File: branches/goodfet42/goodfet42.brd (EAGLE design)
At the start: 47.9 x 19.7 mm, 11 parts, among them U1 F261X---PM64, U2 FT232RL-BASICSSOP

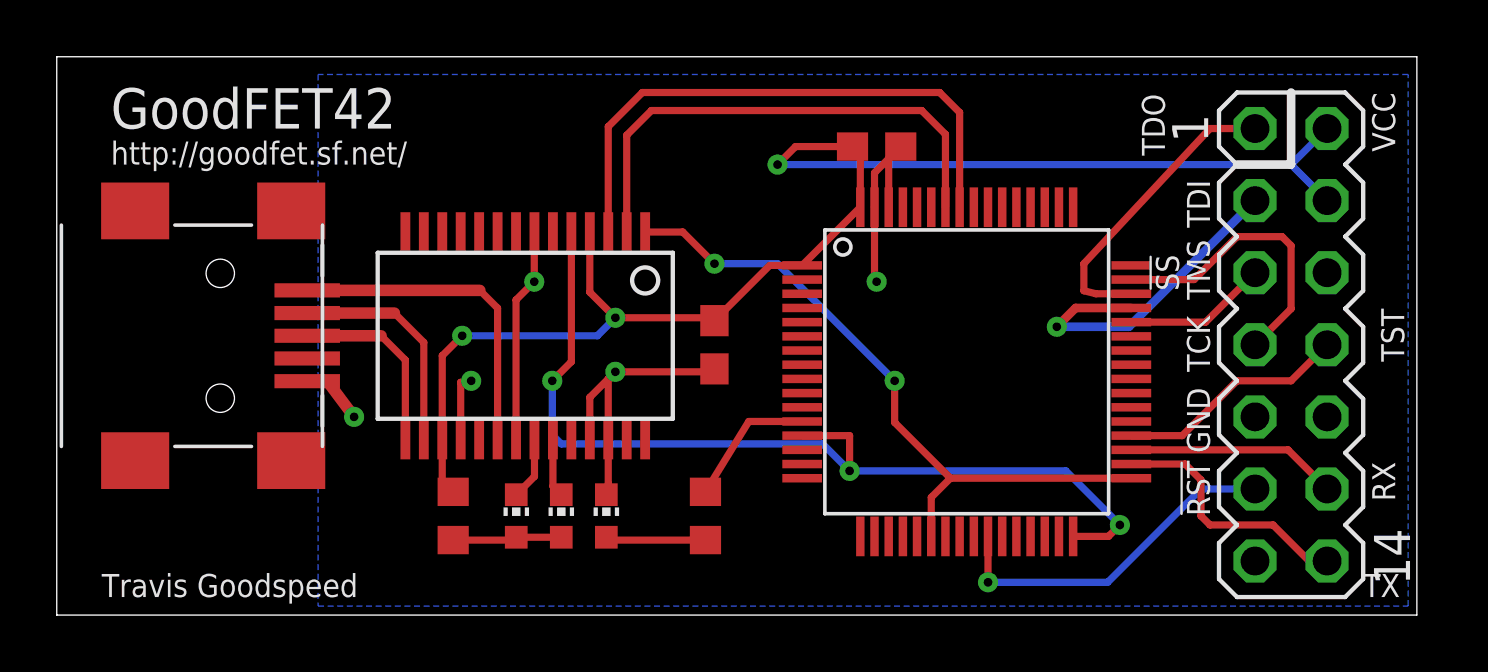
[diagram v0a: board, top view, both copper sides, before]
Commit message: Reinserted names, values in layout.
git-svn-id: https://svn.code.sf.net/p/goodfet/code@1316 12e2690d-a6be-4b82-a7b7-67c4a43b65c8
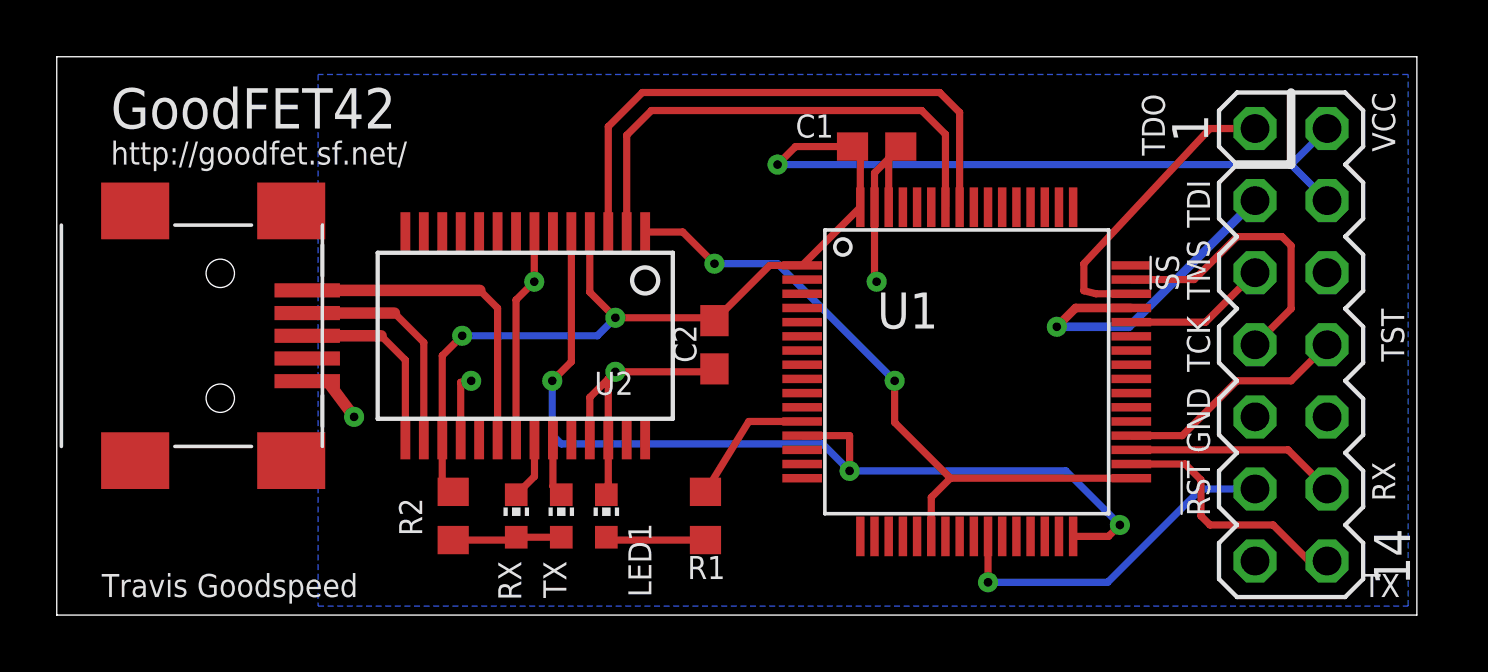
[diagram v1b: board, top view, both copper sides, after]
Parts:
- U1: value F261X---PM64 -> MSP430F2618TPM
- U2: value FT232RL-BASICSSOP -> FT232RL
- renumbered RXLED to RX, TXLED to TX
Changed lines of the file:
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@@
 <?xml version="1.0" encoding="utf-8"?>
 <!DOCTYPE eagle SYSTEM "eagle.dtd">
-<eagle version="6.2">
+<eagle version="6.3">
 <drawing>
 <settings>
@@
 </class>
 </classes>
-<designrules>
+<designrules name="default">
 <description language="de">&lt;b&gt;EAGLE Design Rules&lt;/b&gt;
 &lt;p&gt;
@@
 </autorouter>
 <elements>
-<element name="C1" library="rcl" package="C0603" value="0.1µF" x="28.8925" y="16.51" smashed="yes" rot="R180"/>
-<element name="R1" library="rcl" package="R0603" value="330" x="22.86" y="3.4925" smashed="yes" rot="R90"/>
+<element name="C1" library="rcl" package="C0603" value="0.1µF" x="28.8925" y="16.51" smashed="yes" rot="R180">
+<attribute name="NAME" x="26.035" y="16.8275" size="0.8128" layer="25" font="fixed"/>
+<attribute name="VALUE" x="30.7975" y="18.415" size="0.8128" layer="27" font="fixed" rot="R180"/>
+</element>
+<element name="R1" library="rcl" package="R0603" value="330" x="22.86" y="3.4925" smashed="yes" rot="R90">
+<attribute name="NAME" x="22.225" y="1.27" size="0.8128" layer="25" font="fixed"/>
+<attribute name="VALUE" x="24.13" y="1.27" size="0.8128" layer="27" font="fixed"/>
+</element>
 <element name="LED1" library="led" package="CHIP-LED0603" value="" x="19.3675" y="3.4925" smashed="yes">
+<attribute name="NAME" x="20.955" y="0.635" size="0.8128" layer="25" rot="R90"/>
 <attribute name="VALUE" x="21.2725" y="2.8575" size="1.27" layer="27" rot="R90"/>
 </element>
-<element name="U2" library="SparkFun" package="SSOP28DB" value="FT232RL-BASICSSOP" x="16.51" y="9.8425" smashed="yes" rot="R180"/>
-<element name="RXLED" library="led" package="CHIP-LED0603" value="" x="16.1925" y="3.4925" smashed="yes">
+<element name="U2" library="SparkFun" package="SSOP28DB" value="FT232RL" x="16.51" y="9.8425" smashed="yes" rot="R180">
+<attribute name="NAME" x="20.32" y="8.5725" size="0.8128" layer="25" font="fixed" rot="R180"/>
+<attribute name="VALUE" x="11.7475" y="11.43" size="0.8128" layer="27" font="fixed"/>
+</element>
+<element name="RX" library="led" package="CHIP-LED0603" value="" x="16.1925" y="3.4925" smashed="yes">
+<attribute name="NAME" x="15.5575" y="1.905" size="0.8128" layer="25" font="fixed" rot="R270"/>
 <attribute name="VALUE" x="18.0975" y="2.8575" size="1.27" layer="27" rot="R90"/>
 </element>
-<element name="TXLED" library="led" package="CHIP-LED0603" value="" x="17.78" y="3.4925" smashed="yes">
+<element name="TX" library="led" package="CHIP-LED0603" value="" x="17.78" y="3.4925" smashed="yes">
+<attribute name="NAME" x="17.145" y="1.905" size="0.8128" layer="25" font="fixed" rot="R270"/>
 <attribute name="VALUE" x="19.685" y="2.8575" size="1.27" layer="27" rot="R90"/>
 </element>
-<element name="R2" library="rcl" package="R0603" value="330" x="13.97" y="3.4925" smashed="yes" rot="R90"/>
-<element name="C2" library="rcl" package="C0603" value="0.1µF" x="23.1775" y="9.525" smashed="yes" rot="R90"/>
+<element name="R2" library="rcl" package="R0603" value="330" x="13.97" y="3.4925" smashed="yes" rot="R90">
+<attribute name="NAME" x="12.065" y="4.1275" size="0.8128" layer="25" font="fixed" rot="R270"/>
+<attribute name="VALUE" x="14.9225" y="1.905" size="0.8128" layer="27" rot="R180"/>
+</element>
+<element name="C2" library="rcl" package="C0603" value="0.1µF" x="23.1775" y="9.525" smashed="yes" rot="R90">
+<attribute name="NAME" x="22.5425" y="8.89" size="0.8128" layer="25" font="fixed" rot="R90"/>
+<attribute name="VALUE" x="25.0825" y="7.62" size="0.8128" layer="27" font="fixed" rot="R90"/>
+</element>
 <element name="JTAG" library="con-lstb" package="MA07-2" value="" x="43.4975" y="9.525" smashed="yes" rot="R270">
 <attribute name="VALUE" x="39.3065" y="12.065" size="1.27" layer="27" ratio="10" rot="R270"/>
 </element>
-<element name="U1" library="TI_MSP430_v13" package="PM/PAG64" value="F261X---PM64" x="32.0675" y="8.5725" smashed="yes"/>
+<element name="U1" library="TI_MSP430_v13" package="PM/PAG64" value="MSP430F2618TPM" x="32.0675" y="8.5725" smashed="yes">
+<attribute name="VALUE" x="27.2575" y="6.575" size="0.8128" layer="27" font="fixed" ratio="10"/>
+<attribute name="NAME" x="28.9125" y="10.0975" size="1.27" layer="25" font="fixed" ratio="10"/>
+</element>
 <element name="CN1" library="adafruit" package="USB-MINIB" value="" x="4.7625" y="9.8425" smashed="yes" rot="R270">
 <attribute name="VALUE" x="-1.5875" y="13.1525" size="1.27" layer="27" rot="R270"/>
@@
 <signal name="N$6">
 <contactref element="U2" pad="22"/>
-<contactref element="RXLED" pad="C"/>
+<contactref element="RX" pad="C"/>
 <wire x1="16.835" y1="4.885" x2="16.835" y2="6.1865" width="0.254" layer="1"/>
 <wire x1="16.1925" y1="4.2425" x2="16.835" y2="4.885" width="0.254" layer="1"/>
@@
 <signal name="N$7">
 <contactref element="U2" pad="23"/>
-<contactref element="TXLED" pad="C"/>
+<contactref element="TX" pad="C"/>
 <wire x1="17.485" y1="4.5375" x2="17.485" y2="6.1865" width="0.254" layer="1"/>
 <wire x1="17.485" y1="4.5375" x2="17.78" y2="4.2425" width="0.254" layer="1"/>
 </signal>
 <signal name="N$8">
-<contactref element="RXLED" pad="A"/>
-<contactref element="TXLED" pad="A"/>
+<contactref element="RX" pad="A"/>
+<contactref element="TX" pad="A"/>
 <contactref element="R2" pad="1"/>
 <wire x1="13.97" y1="2.6425" x2="16.0925" y2="2.6425" width="0.254" layer="1"/>
